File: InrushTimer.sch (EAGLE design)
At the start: 71 parts, among them IC1 TLC272D, IC2 555, IC3 4076N, Q2 TRANSISTOR-FET_2N7002, Q3 TRANSISTOR-FET_2N7002, Q4 TRANSISTOR-FET_2N7002, Q5 TRANSISTOR-FET_2N7002, Q6 DIODES_ZTX451DIODES_ZTX451_0_0, T1 MMBTA05, U1 ROHM_BY_ELEMENT14_BATCH_1_BU4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

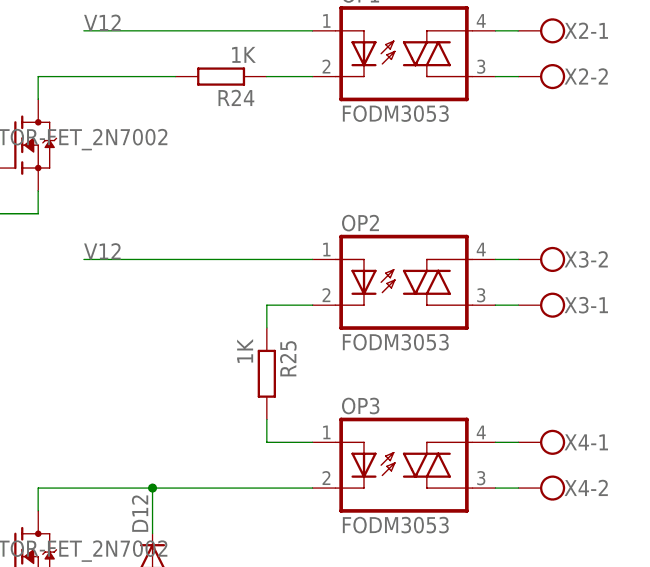
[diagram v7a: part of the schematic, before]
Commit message: ayed out the timer - starting on the D types. Fixed incorrect gate capacitance.
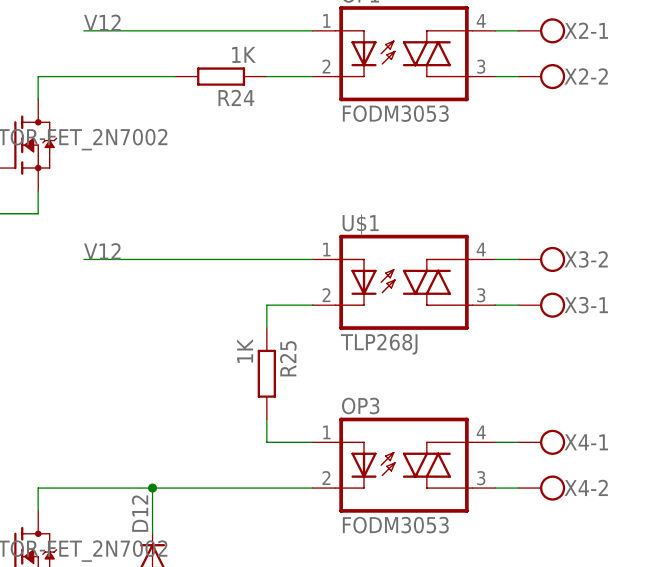
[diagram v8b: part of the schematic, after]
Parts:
- removed OP2: FODM3053, SHoleLib:FODM3053
- added U$1: TLP268J, SHoleLib:TLP268J
- R17: device rcl:R-EU_0207/7 -> rcl:R-EU_0207/2V
- R9: device rcl:R-EU_0204/7 -> rcl:R-EU_0207/7
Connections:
- net N$17: now also U$1.C; no longer OP2.C
- net N$20: now also U$1.A2; no longer OP2.A2
- net N$21: now also U$1.A1; no longer OP2.A1
- net V12: now also U$1.A; no longer OP2.A
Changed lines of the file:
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@@
 <part name="R8" library="rcl" deviceset="R-EU_" device="0207/2V" value="22K"/>
 <part name="D5" library="diode" deviceset="DIODE-" device="DP41-10V" value="1n4001"/>
-<part name="R9" library="rcl" deviceset="R-EU_" device="0204/7" value="9.1M"/>
+<part name="R9" library="rcl" deviceset="R-EU_" device="0207/7" value="9.1M"/>
 <part name="R11" library="rcl" deviceset="R-EU_" device="0207/2V" value="200K"/>
 <part name="R12" library="rcl" deviceset="R-EU_" device="0207/2V" value="100K"/>
@@
 <part name="C13" library="rcl" deviceset="C-EU" device="C1206K" value="2.2uF"/>
 <part name="R16" library="rcl" deviceset="R-EU_" device="R0402" value="1K"/>
-<part name="R17" library="rcl" deviceset="R-EU_" device="0207/7" value="51K"/>
+<part name="R17" library="rcl" deviceset="R-EU_" device="0207/2V" value="51K"/>
 <part name="C12" library="rcl" deviceset="C-EU" device="050-024X044" value="100nF"/>
 <part name="R15" library="pot" deviceset="TRIM_EU-" device="CA6H_MOD" value="220K"/>
@@
 <part name="R10" library="rcl" deviceset="R-EU_" device="0207/10" value="10K"/>
 <part name="OP3" library="SHoleLib" deviceset="FODM3053" device=""/>
-<part name="OP2" library="SHoleLib" deviceset="FODM3053" device=""/>
 <part name="OP1" library="SHoleLib" deviceset="FODM3053" device=""/>
 <part name="U1" library="InrushTimer" deviceset="ROHM_BY_ELEMENT14_BATCH_1_BU48XXG" device=""/>
@@
 <part name="D2" library="diode" deviceset="ZENER-DIODE" device="DO34-7" value="BZX55C5V6"/>
 <part name="D3" library="diode" deviceset="DIODE-" device="DO34-7" value="5082-2800"/>
+<part name="U$1" library="SHoleLib" deviceset="TLP268J" device=""/>
 </parts>
 <sheets>
@@
 <instance part="R10" gate="G$1" x="-2.54" y="78.74" rot="R180"/>
 <instance part="OP3" gate="G$1" x="368.3" y="-12.7"/>
-<instance part="OP2" gate="G$1" x="368.3" y="7.62"/>
 <instance part="OP1" gate="G$1" x="368.3" y="33.02"/>
 <instance part="U1" gate="G$1" x="-20.32" y="-81.28"/>
@@
 <instance part="D2" gate="G$1" x="7.62" y="-88.9" rot="R90"/>
 <instance part="D3" gate="G$1" x="-22.86" y="60.96" rot="R270"/>
+<instance part="U$1" gate="G$1" x="368.3" y="7.62"/>
 </instances>
 <busses>
@@
 <wire x1="358.14" y1="10.16" x2="332.74" y2="10.16" width="0.1524" layer="91"/>
 <label x="332.74" y="10.16" size="1.778" layer="95"/>
-<pinref part="OP2" gate="G$1" pin="A"/>
+<pinref part="U$1" gate="G$1" pin="A"/>
 </segment>
 </net>
@@
 <wire x1="358.14" y1="5.08" x2="353.06" y2="5.08" width="0.1524" layer="91"/>
 <wire x1="353.06" y1="5.08" x2="353.06" y2="2.54" width="0.1524" layer="91"/>
-<pinref part="OP2" gate="G$1" pin="C"/>
+<pinref part="U$1" gate="G$1" pin="C"/>
 </segment>
 </net>
@@
 <pinref part="X3" gate="-2" pin="KL"/>
 <wire x1="381" y1="10.16" x2="378.46" y2="10.16" width="0.1524" layer="91"/>
-<pinref part="OP2" gate="G$1" pin="A2"/>
+<pinref part="U$1" gate="G$1" pin="A2"/>
 </segment>
 </net>
@@
 <pinref part="X3" gate="-1" pin="KL"/>
 <wire x1="381" y1="5.08" x2="378.46" y2="5.08" width="0.1524" layer="91"/>
-<pinref part="OP2" gate="G$1" pin="A1"/>
-</segment>
-</net>
+<pinref part="U$1" gate="G$1" pin="A1"/>
+</segment>
+</net>
